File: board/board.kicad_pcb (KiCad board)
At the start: 2 copper layers, 50.8 x 22.9 mm, 16 parts, among them J1 MOTION DETECTOR, J2 EXT BUTTON, U3 ATTINY85-20PU

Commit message: Revision
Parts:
- R1: value 22.6K -> 22.1K
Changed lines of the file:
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@@
       (effects (font (size 1 1) (thickness 0.15)))
     )
-    (fp_text value 22.6K (at 0.25 1.5) (layer F.Fab)
+    (fp_text value 22.1K (at 0.25 1.5) (layer F.Fab)
       (effects (font (size 1 1) (thickness 0.15)))
     )
@@
   (gr_line (start 160.02 102.87) (end 114.3 102.87) (angle 90) (layer Edge.Cuts) (width 0.1))
   (gr_line (start 162.56 123.19) (end 162.56 105.41) (angle 90) (layer Edge.Cuts) (width 0.1))
-  (segment (start 142.7 115.6) (end 142.25 116.05) (width 0.25) (layer F.Cu) (net 1))
-  (segment (start 142.25 116.05) (end 142.25 120.5) (width 0.25) (layer F.Cu) (net 1))
-  (segment (start 142.25 120.66) (end 146.05 124.46) (width 0.25) (layer B.Cu) (net 1))
+  (segment (start 142.7 115.6) (end 142.25 116.05) (width 0.25) (layer F.Cu) (net 1) (status 30))
+  (segment (start 142.25 116.05) (end 142.25 120.5) (width 0.25) (layer F.Cu) (net 1) (status 10))
+  (segment (start 142.25 120.66) (end 146.05 124.46) (width 0.25) (layer B.Cu) (net 1) (status 20))
   (segment (start 142.25 120.5) (end 142.25 120.66) (width 0.25) (layer B.Cu) (net 1))
   (via (at 142.25 120.5) (size 0.6) (drill 0.4) (layers F.Cu B.Cu) (net 1))
   (segment (start 145.96 124.46) (end 146.05 124.46) (width 0.25) (layer F.Cu) (net 1) (status 30))
-  (segment (start 142.7 114) (end 142.25 114) (width 0.25) (layer F.Cu) (net 2))
-  (segment (start 142.25 114) (end 141.5 114.75) (width 0.25) (layer F.Cu) (net 2))
-  (segment (start 141.5 122.45) (end 143.51 124.46) (width 0.25) (layer B.Cu) (net 2))
+  (segment (start 142.7 114) (end 142.25 114) (width 0.25) (layer F.Cu) (net 2) (status 30))
+  (segment (start 142.25 114) (end 141.5 114.75) (width 0.25) (layer F.Cu) (net 2) (status 10))
+  (segment (start 141.5 122.45) (end 143.51 124.46) (width 0.25) (layer B.Cu) (net 2) (status 20))
   (segment (start 141.5 121) (end 141.5 122.45) (width 0.25) (layer B.Cu) (net 2))
   (via (at 141.5 121) (size 0.6) (drill 0.4) (layers F.Cu B.Cu) (net 2))
@@
   (segment (start 131.8 112.4) (end 128.27 108.87) (width 0.5) (layer F.Cu) (net 4) (status 10))
   (segment (start 128.27 108.87) (end 128.27 104.14) (width 0.5) (layer F.Cu) (net 4) (status 20))
-  (segment (start 154.25 115.65) (end 154.25 116.1) (width 0.5) (layer F.Cu) (net 5))
-  (segment (start 154.25 116.1) (end 152 118.35) (width 0.5) (layer F.Cu) (net 5))
+  (segment (start 154.25 115.65) (end 154.25 116.1) (width 0.5) (layer F.Cu) (net 5) (status 30))
+  (segment (start 154.25 116.1) (end 152 118.35) (width 0.5) (layer F.Cu) (net 5) (status 30))
   (segment (start 120.65 124.35) (end 120.65 124.46) (width 0.5) (layer F.Cu) (net 5) (status 30))
   (segment (start 148.1 108) (end 149 107.1) (width 0.25) (layer F.Cu) (net 6) (status 10))
@@
   (segment (start 121.4 121.17) (end 118.11 124.46) (width 0.25) (layer F.Cu) (net 16) (status 30))
   (segment (start 118.15 124.42) (end 118.11 124.46) (width 0.25) (layer F.Cu) (net 16) (status 30))
-  (segment (start 159.75 114.21) (end 160.01 114.21) (width 0.25) (layer B.Cu) (net 17))
-  (segment (start 160.01 114.21) (end 161.1 115.3) (width 0.25) (layer B.Cu) (net 17))
+  (segment (start 159.75 114.21) (end 160.01 114.21) (width 0.25) (layer B.Cu) (net 17) (status 30))
+  (segment (start 160.01 114.21) (end 161.1 115.3) (width 0.25) (layer B.Cu) (net 17) (status 10))
   (segment (start 160.5 120) (end 154.25 120) (width 0.25) (layer F.Cu) (net 17))
   (via (at 160.5 120) (size 0.6) (drill 0.4) (layers F.Cu B.Cu) (net 17))
   (segment (start 161.1 119.4) (end 160.5 120) (width 0.25) (layer B.Cu) (net 17))
   (segment (start 161.1 115.3) (end 161.1 119.4) (width 0.25) (layer B.Cu) (net 17))
-  (segment (start 159.75 114.21) (end 159.79 114.21) (width 0.25) (layer F.Cu) (net 17))
-  (segment (start 159.79 114.21) (end 161.5 112.5) (width 0.25) (layer F.Cu) (net 17))
-  (segment (start 156.53 107) (end 153.67 104.14) (width 0.25) (layer F.Cu) (net 17))
+  (segment (start 159.75 114.21) (end 159.79 114.21) (width 0.25) (layer F.Cu) (net 17) (status 30))
+  (segment (start 159.79 114.21) (end 161.5 112.5) (width 0.25) (layer F.Cu) (net 17) (status 10))
+  (segment (start 156.53 107) (end 153.67 104.14) (width 0.25) (layer F.Cu) (net 17) (status 20))
   (segment (start 157.75 107) (end 156.53 107) (width 0.25) (layer F.Cu) (net 17))
   (segment (start 161.5 110.75) (end 157.75 107) (width 0.25) (layer F.Cu) (net 17))
   (segment (start 161.5 112.5) (end 161.5 110.75) (width 0.25) (layer F.Cu) (net 17))
-  (segment (start 154.25 118.35) (end 154.25 120) (width 0.25) (layer F.Cu) (net 17))
+  (segment (start 154.25 118.35) (end 154.25 120) (width 0.25) (layer F.Cu) (net 17) (status 10))
   (segment (start 154.25 120) (end 150.25 120) (width 0.25) (layer F.Cu) (net 17))
   (segment (start 148.135 117.885) (end 150.25 120) (width 0.25) (layer F.Cu) (net 17))
@@
   (segment (start 159.96 114.21) (end 159.75 114.21) (width 0.25) (layer B.Cu) (net 17) (status 30))
   (segment (start 148.135 116.7) (end 148.135 117.385) (width 0.25) (layer F.Cu) (net 17) (status 30))
-  (segment (start 152 115.65) (end 152.25 115.4) (width 0.25) (layer F.Cu) (net 18))
-  (segment (start 152.25 115.4) (end 152.25 114) (width 0.25) (layer F.Cu) (net 18))
-  (segment (start 152.25 114) (end 157 114) (width 0.25) (layer B.Cu) (net 18))
+  (segment (start 152 115.65) (end 152.25 115.4) (width 0.25) (layer F.Cu) (net 18) (status 30))
+  (segment (start 152.25 115.4) (end 152.25 114) (width 0.25) (layer F.Cu) (net 18) (status 10))
+  (segment (start 152.25 114) (end 157 114) (width 0.25) (layer B.Cu) (net 18) (status 20))
   (via (at 152.25 114) (size 0.6) (drill 0.4) (layers F.Cu B.Cu) (net 18))
-  (segment (start 157 114) (end 157.21 114.21) (width 0.25) (layer B.Cu) (net 18))
-  (segment (start 145.595 116.7) (end 145.595 115.905) (width 0.25) (layer F.Cu) (net 18))
-  (segment (start 146.25 115.25) (end 151.6 115.25) (width 0.25) (layer F.Cu) (net 18))
+  (segment (start 157 114) (end 157.21 114.21) (width 0.25) (layer B.Cu) (net 18) (status 30))
+  (segment (start 145.595 116.7) (end 145.595 115.905) (width 0.25) (layer F.Cu) (net 18) (status 10))
+  (segment (start 146.25 115.25) (end 151.6 115.25) (width 0.25) (layer F.Cu) (net 18) (status 20))
   (segment (start 145.595 115.905) (end 146.25 115.25) (width 0.25) (layer F.Cu) (net 18))
-  (segment (start 151.6 115.25) (end 152 115.65) (width 0.25) (layer F.Cu) (net 18))
-  (segment (start 157.21 114.21) (end 156.46 114.21) (width 0.25) (layer B.Cu) (net 18))
-  (segment (start 156.46 114.21) (end 155.25 113) (width 0.25) (layer B.Cu) (net 18))
-  (segment (start 155.25 105.1) (end 156.21 104.14) (width 0.25) (layer B.Cu) (net 18))
+  (segment (start 151.6 115.25) (end 152 115.65) (width 0.25) (layer F.Cu) (net 18) (status 30))
+  (segment (start 157.21 114.21) (end 156.46 114.21) (width 0.25) (layer B.Cu) (net 18) (status 30))
+  (segment (start 156.46 114.21) (end 155.25 113) (width 0.25) (layer B.Cu) (net 18) (status 10))
+  (segment (start 155.25 105.1) (end 156.21 104.14) (width 0.25) (layer B.Cu) (net 18) (status 20))
   (segment (start 155.25 113) (end 155.25 105.1) (width 0.25) (layer B.Cu) (net 18))
   (zone (net 3) (net_name GND) (layer B.Cu) (hatch edge 0.508)

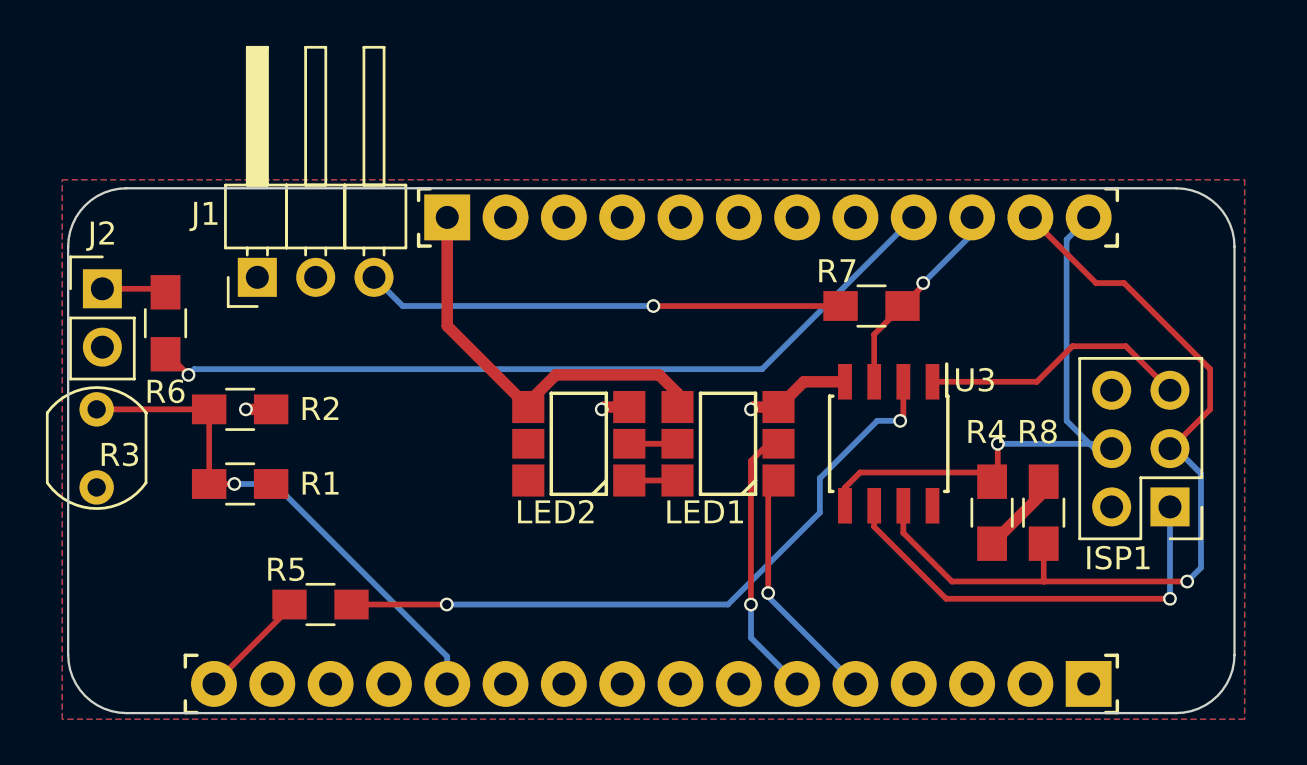
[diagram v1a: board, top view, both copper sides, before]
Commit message: Add power button and GPIO16 reset jumper
* Remove redundant resistors
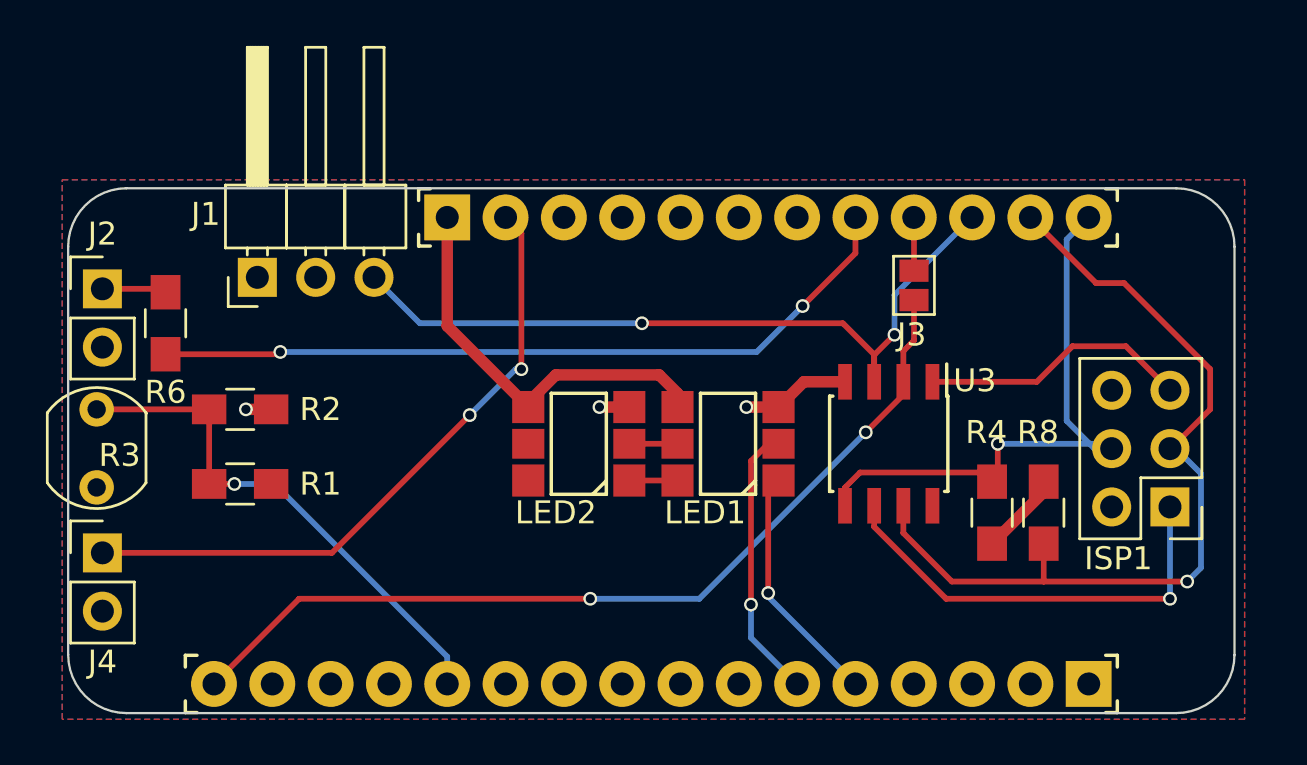
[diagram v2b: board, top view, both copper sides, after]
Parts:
- removed R5, R7: 1K, Resistors_SMD:R_0805_HandSoldering
- added J3: GS2, Connectors:GS2, F.Cu at (148.6, 107.1)
- added J4: ~POWER, Pin_Headers:Pin_Header_Straight_1x02_Pitch2.54mm, F.Cu at (113.2, 118.8)
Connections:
- J1 pad 3: Net-(J1-Pad3) -> /D5
- JP3 pad 2: (no net) -> /EN
- JP3 pad 8: (no net) -> /D9
- R6 pad 2: /D6 -> /D9
- U3 pad 2: Net-(R5-Pad1) -> /~RESET
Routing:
- net /~RESET: track 4.88 -> 39.6 mm, vias 0 -> 2
- net /D9: track 0.00 -> 33.5 mm, vias 0 -> 2
- net /D6: track 35.8 -> 2.32 mm, vias 1 -> 0
- net Net-(R5-Pad1): track 29.8 -> 0.00 mm, vias 2 -> 0
- net /EN: track 0.00 -> 28.5 mm, vias 0 -> 2
- net /D5: track 8.95 -> 34.6 mm, vias 1 -> 2
- net Net-(J1-Pad3): track 20.8 -> 0.00 mm, vias 1 -> 0

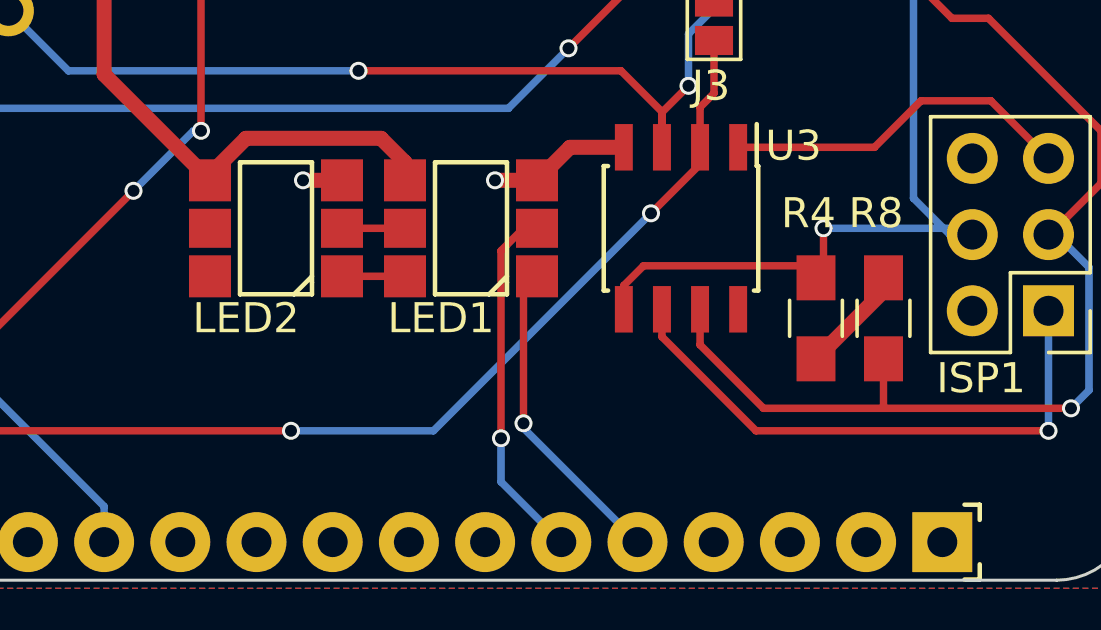
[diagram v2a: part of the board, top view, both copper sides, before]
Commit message: Clean up fab layer
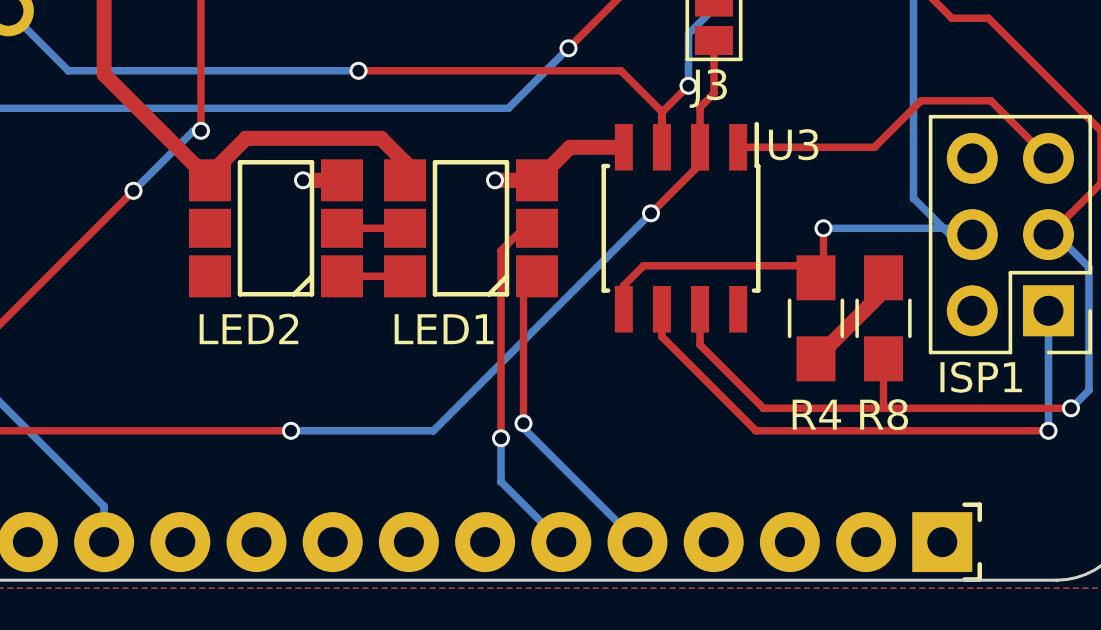
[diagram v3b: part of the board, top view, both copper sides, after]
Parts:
- U3: value ATTINY85-20PU -> ATTINY85

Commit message: Board updates
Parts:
- added REF***: OSHW-Symbol_6.7x6mm_SilkScreen, Symbols:OSHW-Symbol_6.7x6mm_SilkScreen, F.Cu at (121.4, 114.8)
- moved R3 48.7 mm to (161.5, 116.5), turned to 90 degrees
- moved R2 40.8 mm to (159.5, 119.2), turned to 180 degrees
- moved R1 40.6 mm to (159.5, 121.2), turned to 180 degrees
- moved R4 15.3 mm to (140.2, 107.3), turned to 0 degrees
- moved ISP1 8.78 mm to (160.5, 108.0), turned to 270 degrees
- moved R8 5.17 mm to (152.6, 112.1), turned to 90 degrees
- moved U3 0.75 mm to (146.8, 114.0)
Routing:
- net /A0: track 24.0 -> 41.8 mm, vias 1 -> 0
- net /SCL: track 38.5 -> 25.5 mm, vias 1 -> 2
- net /SDA: track 26.2 -> 35.5 mm, vias 1 -> 0
- net VCC: track 3.74 -> 0.11 mm
- net Net-(ISP1-Pad1): track 19.1 -> 22.7 mm
- net Net-(ISP1-Pad5): track 11.8 -> 8.75 mm, vias 0 -> 2
- net /D5: track 34.6 -> 36.8 mm, vias 2 -> 1
- net /~RESET: track 39.6 -> 41.3 mm, vias 2 -> 4
- net GND: track 7.29 -> 6.01 mm
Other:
- board text added: "Wifi Lantern 2017 Steve Pomeroy staticfree.info"
